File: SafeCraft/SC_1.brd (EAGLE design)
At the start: 26 x 25.1 mm, 19 parts, among them IC1 TS555, Q1 DSS20201L-7

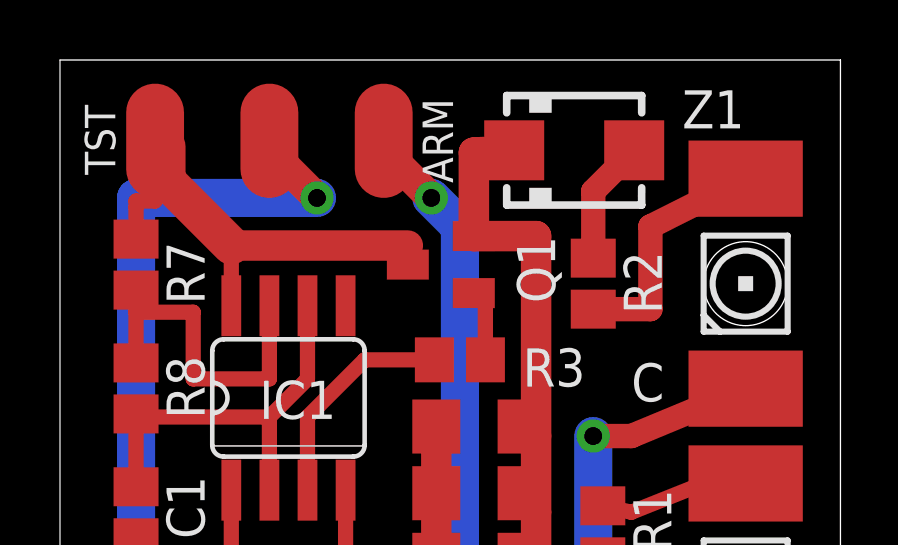
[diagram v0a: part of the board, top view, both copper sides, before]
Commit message: moved a trace slightly
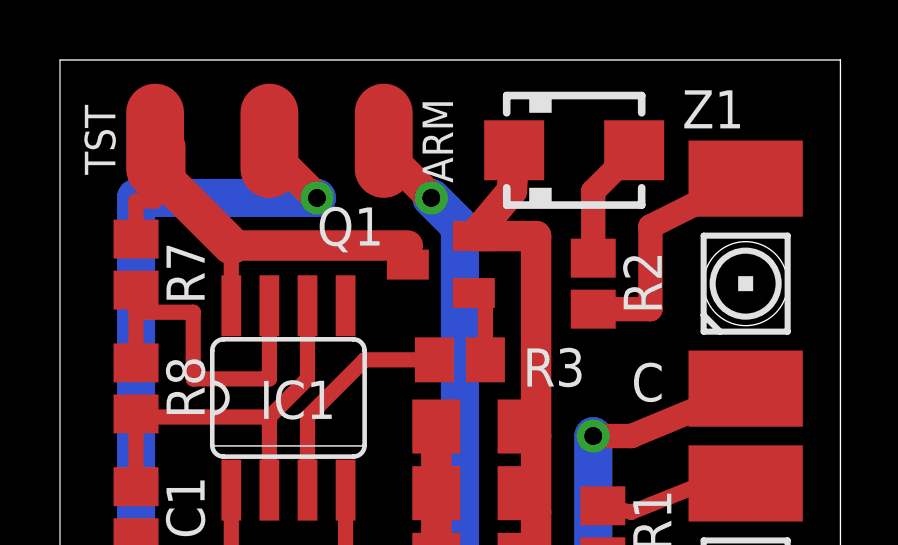
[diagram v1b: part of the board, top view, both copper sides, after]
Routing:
- net N$13: track 19.0 -> 18.2 mm
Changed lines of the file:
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@@
 <layer number="27" name="tValues" color="7" fill="1" visible="yes" active="yes"/>
 <layer number="28" name="bValues" color="7" fill="1" visible="yes" active="yes"/>
-<layer number="29" name="tStop" color="7" fill="3" visible="no" active="yes"/>
-<layer number="30" name="bStop" color="7" fill="6" visible="no" active="yes"/>
+<layer number="29" name="tStop" color="7" fill="3" visible="yes" active="yes"/>
+<layer number="30" name="bStop" color="7" fill="6" visible="yes" active="yes"/>
 <layer number="31" name="tCream" color="7" fill="4" visible="yes" active="yes"/>
 <layer number="32" name="bCream" color="7" fill="5" visible="yes" active="yes"/>
@@
 </element>
 <element name="Q1" library="transistor-npn" package="SOT23-BEC" value="DSS20201L-7" x="12.7" y="18.415" smashed="yes" rot="R90">
-<attribute name="NAME" x="15.24" y="19.3675" size="1.27" layer="25" rot="R270"/>
+<attribute name="NAME" x="8.5725" y="19.05" size="1.27" layer="25"/>
 </element>
 <element name="R4" library="rcl" package="R1206" value="24" x="13.97" y="10.795" smashed="yes"/>
@@
 <element name="Z1" library="diode" package="SMA" value="1SMA5915BT3G" x="17.145" y="22.225" smashed="yes">
 <attribute name="NAME" x="20.745" y="22.955" size="1.27" layer="25" ratio="10"/>
-<attribute name="VALUE" x="14.395" y="18.725" size="1.27" layer="27" ratio="10"/>
 </element>
 <element name="R8" library="rcl" package="R0805" value="750K" x="2.54" y="14.2875" smashed="yes" rot="R270">
@@
 <wire x1="15.392" y1="13.0175" x2="15.875" y2="12.7" width="0.508" layer="1"/>
 <wire x1="15.392" y1="10.795" x2="15.875" y2="10.16" width="0.508" layer="1"/>
-<wire x1="15.145" y1="22.225" x2="13.8" y2="22.15" width="1.016" layer="1"/>
-<wire x1="13.8" y1="22.15" x2="13.8" y2="19.365" width="1.016" layer="1"/>
+<wire x1="15.145" y1="22.225" x2="15.07" y2="20.88" width="1.016" layer="1"/>
+<wire x1="15.07" y1="20.88" x2="13.8" y2="19.365" width="1.016" layer="1"/>
 </signal>
 <signal name="N$5">

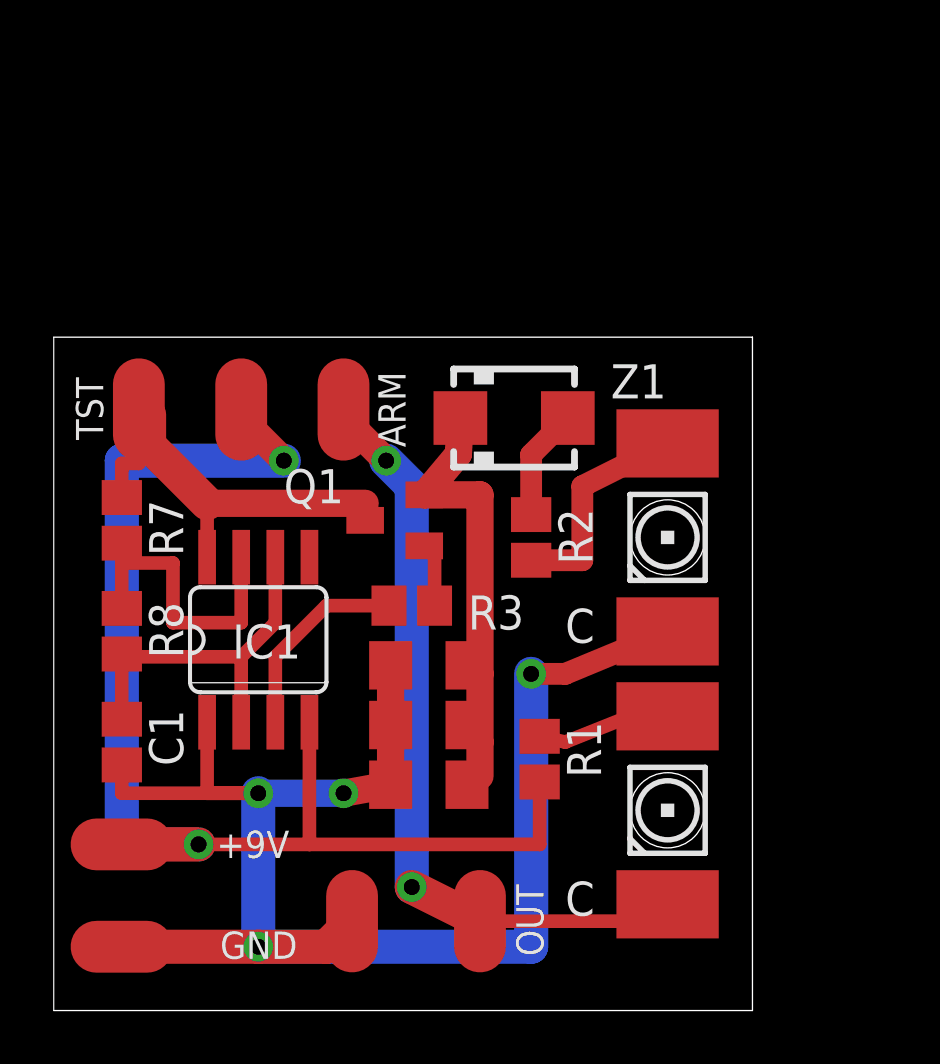
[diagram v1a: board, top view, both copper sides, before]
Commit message: updated schematic for reset line and PNP transistor
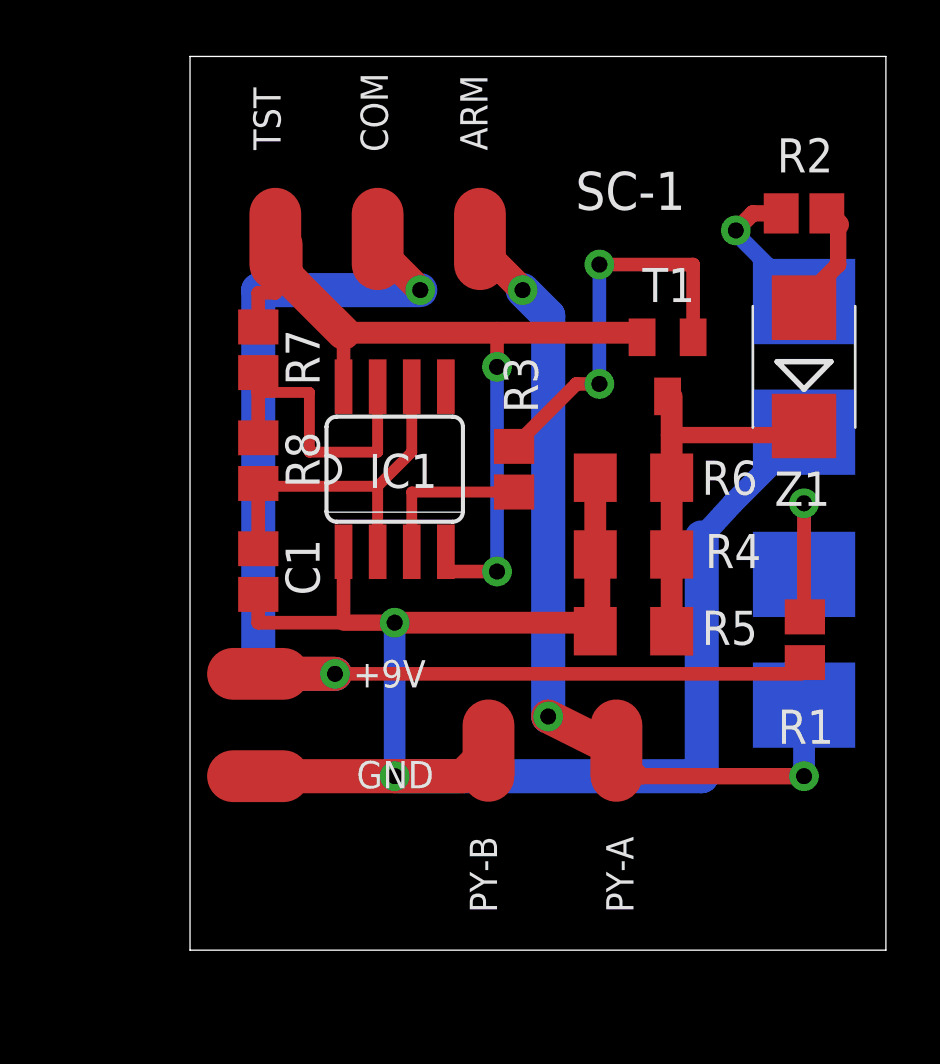
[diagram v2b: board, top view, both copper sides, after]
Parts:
- removed Q1: DSS20201L-7, transistor-npn:SOT23-BEC
- added T1: DSS20200, transistor:SOT23-BEC
- LED1, LED2: device led:P-LCC-2-TOPLED-RG -> led:P-LCC-2
- Z1: device diode:SMA -> diode:SMB
- moved R2 15.8 mm to (27.9, 29.8), turned to 0 degrees
- moved Z1 11.0 mm to (27.9, 24.1), turned to 90 degrees
- moved R1 10.8 mm to (28.0, 14.0)
- moved R6 10.3 mm to (21.6, 20.0)
- moved R4 9.92 mm to (21.6, 17.1)
- moved R5 9.52 mm to (21.6, 14.3)
- moved LED1 8.13 mm to (27.9, 14.0), flipped to the bottom
- moved U$4 8.13 mm to (7.62, 8.89)
- moved C1 8.13 mm to (7.62, 16.5)
- moved IC1 8.13 mm to (12.7, 20.3)
- moved LED2 8.13 mm to (27.9, 24.1), flipped to the bottom
- moved R7 8.13 mm to (7.62, 24.8)
- moved R8 8.13 mm to (7.62, 20.6)
- moved U$3 8.13 mm to (7.62, 12.7)
- moved S2 8.13 mm to (12.1, 28.9)
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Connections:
- removed net N$3: IC1.8, Q1.C, R7.2, S2.P$3
- new net N$1: IC1.4, IC1.8, R7.2, S2.P$3, T1.E
- net +9V: no longer IC1.4
- net N$13: now also T1.C; no longer Q1.E
- net N$9: now also T1.B; no longer Q1.B
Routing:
- net N$1: track 0.00 -> 33.3 mm, vias 0 -> 2
- net N$3: track 17.1 -> 0.00 mm
- net N$9: track 2.38 -> 14.8 mm, vias 0 -> 2
- net GND: track 60.8 -> 66.6 mm, vias 4 -> 2
- net N$13: track 18.2 -> 14.2 mm
- net OUT_A: track 28.8 -> 31.7 mm, vias 2 -> 3
- net N$8: track 8.21 -> 5.65 mm, vias 0 -> 1
- net N$6: track 5.10 -> 6.91 mm, vias 0 -> 1
- net +9V: track 48.2 -> 46.4 mm
- net N$10: track 7.46 -> 6.03 mm
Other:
- board size 26 x 25.1 mm -> 25.9 x 33.3 mm
- board text added: "COM"
- board text added: "PY-A"
- board text added: "PY-B"
- board text added: "SC-1"
- board text removed: "OUT"

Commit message: 
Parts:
- T1: value DSS20200 -> FMMT718TA
- Z1: value 1SMA5915BT3G -> 1SMA5917BT3G
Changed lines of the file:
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@@
 <attribute name="NAME" x="29.0195" y="32.639" size="1.27" layer="25" rot="R180"/>
 </element>
-<element name="Z1" library="diode" package="SMB" value="1SMA5915BT3G" x="27.94" y="24.13" smashed="yes" rot="R90">
+<element name="Z1" library="diode" package="SMB" value="1SMA5917BT3G" x="27.94" y="24.13" smashed="yes" rot="R90">
 <attribute name="NAME" x="28.912" y="20.225" size="1.27" layer="25" ratio="10" rot="R180"/>
 </element>
@@
 <element name="U$3" library="1AA_Stofer" package="SOLDERPAD_NOHOLES" value="SOLDERPAD_NOHOLE" x="7.62" y="12.7"/>
 <element name="U$4" library="1AA_Stofer" package="SOLDERPAD_NOHOLES" value="SOLDERPAD_NOHOLE" x="7.62" y="8.89"/>
-<element name="T1" library="transistor" package="SOT23-BEC" value="DSS20200" x="22.86" y="24.13" smashed="yes" rot="R180">
+<element name="T1" library="transistor" package="SOT23-BEC" value="FMMT718TA" x="22.86" y="24.13" smashed="yes" rot="R180">
 <attribute name="NAME" x="23.876" y="27.813" size="1.27" layer="25" rot="R180"/>
 </element>
